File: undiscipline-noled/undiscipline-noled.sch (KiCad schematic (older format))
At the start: 177 parts, among them J2 USB_B_Micro, SW1 SW_Push, SW10 SW_Push, SW11 SW_Push, SW12 SW_Push, SW13 SW_Push, SW14 SW_Push, SW15 SW_Push, SW16 SW_Push, SW17 SW_Push, SW18 SW_Push, SW19 SW_Push, SW2 SW_Push, SW20 SW_Push, SW21 SW_Push, SW22 SW_Push, SW23 SW_Push, SW24 SW_Push, SW25 SW_Push, SW26 SW_Push, SW27 SW_Push, SW28 SW_Push, SW29 SW_Push, SW3 SW_Push, SW30 SW_Push, SW31 SW_Push, SW32 SW_Push, SW33 SW_Push, SW34 SW_Push, SW35 SW_Push, SW36 SW_Push, SW37 SW_Push, SW38 SW_Push, SW39 SW_Push, SW4 SW_Push, SW40 SW_Push, SW41 SW_Push, SW42 SW_Push, SW43 SW_Push, SW44 SW_Push, SW45 SW_Push, SW46 SW_Push, SW47 SW_Push, SW48 SW_Push, SW49 SW_Push, SW5 SW_Push, SW50 SW_Push, SW51 SW_Push, SW52 SW_Push, SW53 SW_Push, SW54 SW_Push, SW55 SW_Push, SW56 SW_Push, SW57 SW_Push, SW58 SW_Push, SW59 SW_Push, SW6 SW_Push, SW60 SW_Push, SW61 SW_Push, SW62 SW_Push, SW63 SW_Push, SW64 SW_Push, SW65 SW_Push, SW66 SW_Push, SW67 SW_Push, SW68 SW_Push, SW69 SW_Push, SW7 SW_Push, SW70 SW_Push, SW71 SW_Push, SW72 SW_Push, SW73 SW_Push, SW74 SW_Push, SW75 SW_Push, SW8 SW_Push, SW9 SW_Push, U1 ATmega32A-PU, Y1 16MHz

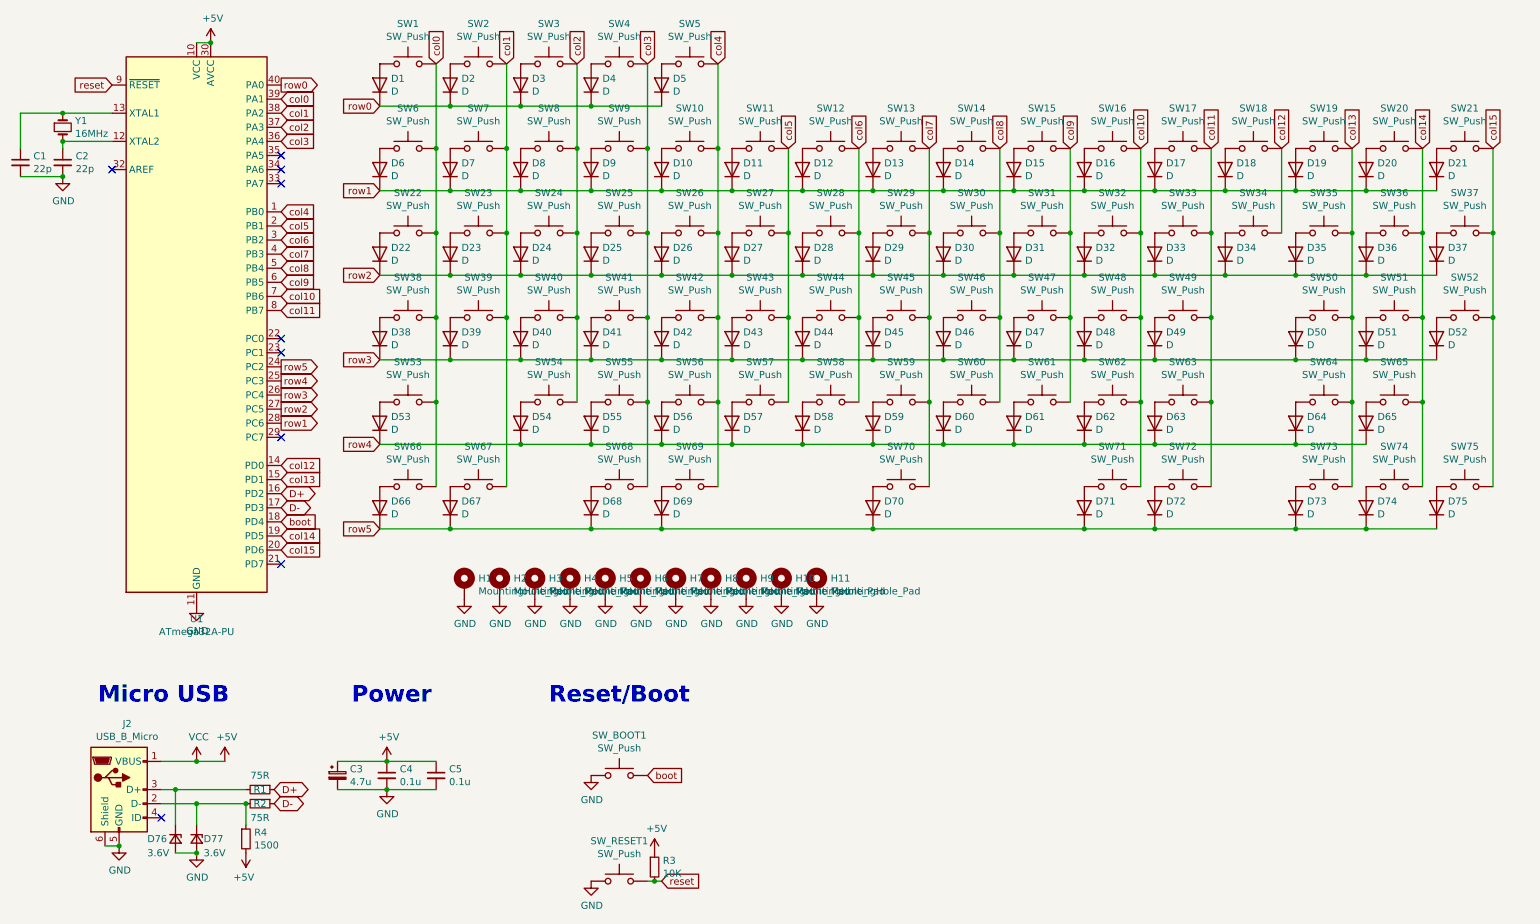
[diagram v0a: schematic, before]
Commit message: Add plates
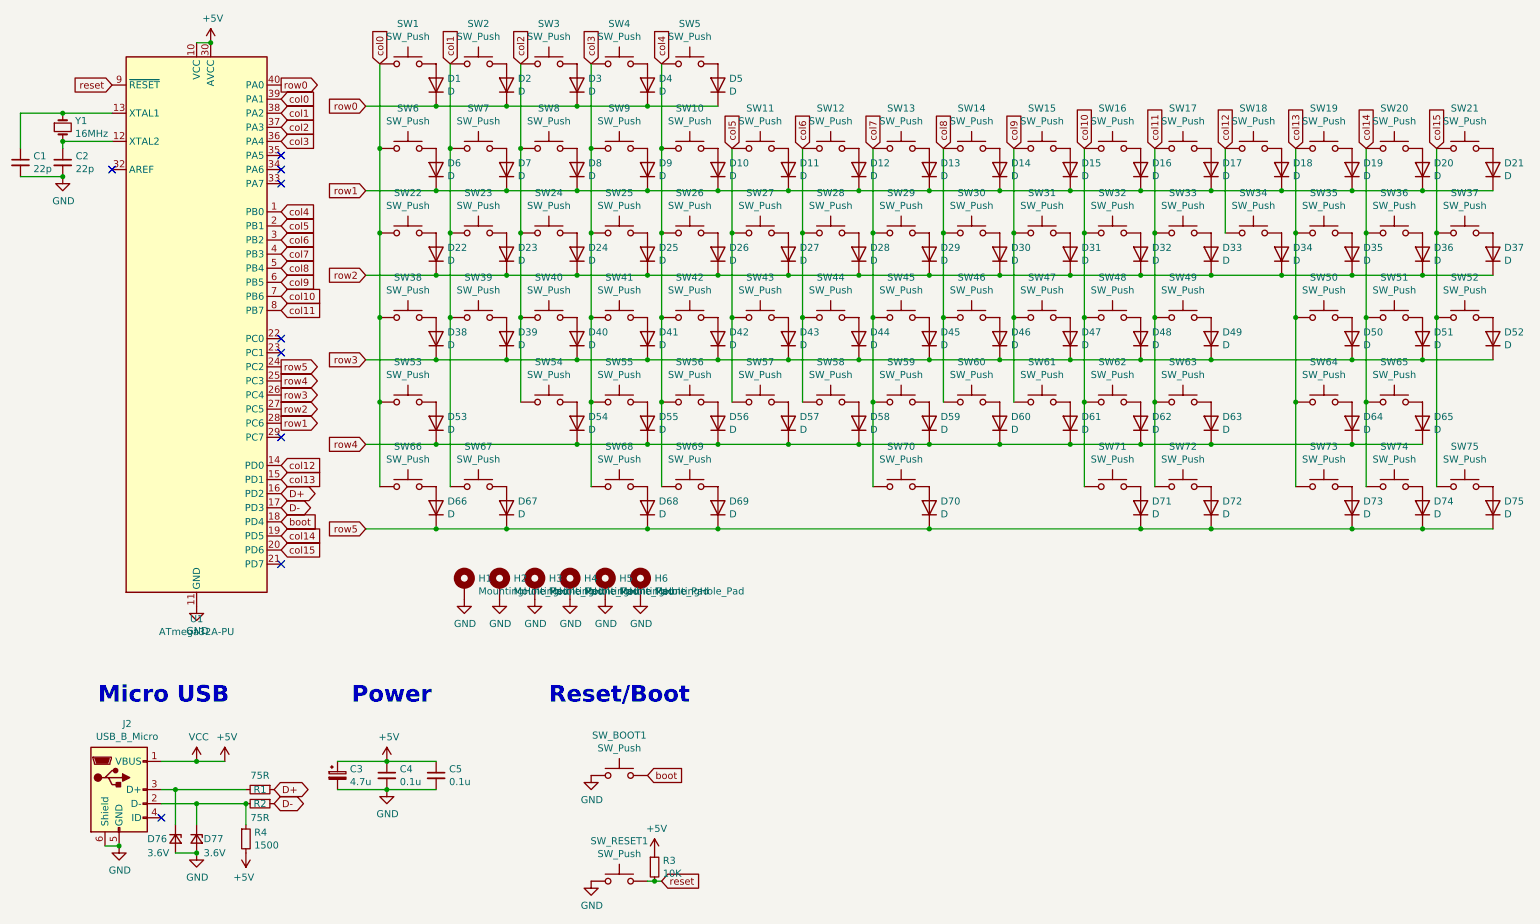
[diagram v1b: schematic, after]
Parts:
- removed H10, H11, H7, H8, H9: MountingHole_Pad, MountingHole:MountingHole_2.2mm_M2_DIN965_Pad_TopBottom, symbol Mechanical:MountingHole_Pad
- SW1, SW10, SW11, SW12, SW13, SW14, SW15, SW16, SW17, SW18, SW2, SW20, SW21, SW23, SW24, SW25, SW26, SW27, SW28, SW29, SW3, SW30, SW31, SW32, SW33, SW34, SW36, SW37, SW39, SW4, SW40, SW41, SW42, SW43, SW44, SW45, SW46, SW47, SW48, SW49, SW5, SW51, SW52, SW53, SW54, SW55, SW56, SW57, SW58, SW59, SW6, SW60, SW61, SW62, SW63, SW65, SW7, SW73, SW74, SW75, SW8, SW9: footprint keyboard-parts:CherryMX_Kailh_Socket -> Button_Switch_Keyboard:SW_Cherry_MX_1.00u_Plate
- SW19: footprint keyboard-parts:CherryMX_Kailh_Socket -> Button_Switch_Keyboard:SW_Cherry_MX_2.00u_Plate
- SW22, SW35: footprint keyboard-parts:CherryMX_Kailh_Socket -> Button_Switch_Keyboard:SW_Cherry_MX_1.50u_Plate
- SW38: footprint keyboard-parts:CherryMX_Kailh_Socket -> Button_Switch_Keyboard:SW_Cherry_MX_1.75u_Plate
- SW50: footprint keyboard-parts:CherryMX_Kailh_Socket -> Button_Switch_Keyboard:SW_Cherry_MX_2.25u_Plate
- SW64: footprint keyboard-parts:CherryMX_Kailh_Socket -> Button_Switch_Keyboard:SW_Cherry_MX_2.75u_Plate
- SW66, SW67, SW68, SW69, SW71, SW72: footprint keyboard-parts:CherryMX_Kailh_Socket -> Button_Switch_Keyboard:SW_Cherry_MX_1.25u_Plate
- SW70: footprint keyboard-parts:CherryMX_Kailh_Socket -> Button_Switch_Keyboard:SW_Cherry_MX_6.25u_Plate
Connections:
- net col0: now also SW1.1, SW22.1, SW38.1, SW53.1, SW6.1, SW66.1; no longer SW1.2, SW22.2, SW38.2, SW53.2, SW6.2, SW66.2
- net col1: now also SW2.1, SW23.1, SW39.1, SW67.1, SW7.1; no longer SW2.2, SW23.2, SW39.2, SW67.2, SW7.2
- net col10: now also SW16.1, SW32.1, SW48.1, SW62.1, SW71.1; no longer SW16.2, SW32.2, SW48.2, SW62.2, SW71.2
- net col11: now also SW17.1, SW33.1, SW49.1, SW63.1, SW72.1; no longer SW17.2, SW33.2, SW49.2, SW63.2, SW72.2
- net col12: now also SW18.1, SW34.1; no longer SW18.2, SW34.2
- net col13: now also SW19.1, SW35.1, SW50.1, SW64.1, SW73.1; no longer SW19.2, SW35.2, SW50.2, SW64.2, SW73.2
- net col14: now also SW20.1, SW36.1, SW51.1, SW65.1, SW74.1; no longer SW20.2, SW36.2, SW51.2, SW65.2, SW74.2
- net col15: now also SW21.1, SW37.1, SW52.1, SW75.1; no longer SW21.2, SW37.2, SW52.2, SW75.2
- net col2: now also SW24.1, SW3.1, SW40.1, SW54.1, SW8.1; no longer SW24.2, SW3.2, SW40.2, SW54.2, SW8.2
- net col3: now also SW25.1, SW4.1, SW41.1, SW55.1, SW68.1, SW9.1; no longer SW25.2, SW4.2, SW41.2, SW55.2, SW68.2, SW9.2
- net col4: now also SW10.1, SW26.1, SW42.1, SW5.1, SW56.1, SW69.1; no longer SW10.2, SW26.2, SW42.2, SW5.2, SW56.2, SW69.2
- net col5: now also SW11.1, SW27.1, SW43.1, SW57.1; no longer SW11.2, SW27.2, SW43.2, SW57.2
- net col6: now also SW12.1, SW28.1, SW44.1, SW58.1; no longer SW12.2, SW28.2, SW44.2, SW58.2
- net col7: now also SW13.1, SW29.1, SW45.1, SW59.1, SW70.1; no longer SW13.2, SW29.2, SW45.2, SW59.2, SW70.2
- net col8: now also SW14.1, SW30.1, SW46.1, SW60.1; no longer SW14.2, SW30.2, SW46.2, SW60.2
- net col9: now also SW15.1, SW31.1, SW47.1, SW61.1; no longer SW15.2, SW31.2, SW47.2, SW61.2
- net at D6.2 (A): now also SW6.2; no longer SW6.1
- net at D7.2 (A): now also SW7.2; no longer SW7.1
- net at D8.2 (A): now also SW8.2; no longer SW8.1
- net at D9.2 (A): now also SW9.2; no longer SW9.1
- net at D10.2 (A): now also SW10.2; no longer SW10.1
- net at D11.2 (A): now also SW11.2; no longer SW11.1
- net at D12.2 (A): now also SW12.2; no longer SW12.1
- net at D13.2 (A): now also SW13.2; no longer SW13.1
- net at D14.2 (A): now also SW14.2; no longer SW14.1
- net at D15.2 (A): now also SW15.2; no longer SW15.1
- net at D16.2 (A): now also SW16.2; no longer SW16.1
- net at D17.2 (A): now also SW17.2; no longer SW17.1
- net at D18.2 (A): now also SW18.2; no longer SW18.1
- net at D19.2 (A): now also SW19.2; no longer SW19.1
- net at D20.2 (A): now also SW20.2; no longer SW20.1
- net at D22.2 (A): now also SW22.2; no longer SW22.1
- net at D23.2 (A): now also SW23.2; no longer SW23.1
- net at D24.2 (A): now also SW24.2; no longer SW24.1
- net at D25.2 (A): now also SW25.2; no longer SW25.1
- net at D26.2 (A): now also SW26.2; no longer SW26.1
- net at D27.2 (A): now also SW27.2; no longer SW27.1
- net at D28.2 (A): now also SW28.2; no longer SW28.1
- net at D29.2 (A): now also SW29.2; no longer SW29.1
- net at D30.2 (A): now also SW30.2; no longer SW30.1
- net at D31.2 (A): now also SW31.2; no longer SW31.1
- net at D32.2 (A): now also SW32.2; no longer SW32.1
- net at D33.2 (A): now also SW33.2; no longer SW33.1
- net at D34.2 (A): now also SW34.2; no longer SW34.1
- net at D35.2 (A): now also SW35.2; no longer SW35.1
- net at D36.2 (A): now also SW36.2; no longer SW36.1
- net at D38.2 (A): now also SW38.2; no longer SW38.1
- net at D39.2 (A): now also SW39.2; no longer SW39.1
- net at D40.2 (A): now also SW40.2; no longer SW40.1
- net at D41.2 (A): now also SW41.2; no longer SW41.1
- net at D42.2 (A): now also SW42.2; no longer SW42.1
- net at D43.2 (A): now also SW43.2; no longer SW43.1
- net at D44.2 (A): now also SW44.2; no longer SW44.1
- net at D45.2 (A): now also SW45.2; no longer SW45.1
- net at D46.2 (A): now also SW46.2; no longer SW46.1
- net at D47.2 (A): now also SW47.2; no longer SW47.1
- net at D48.2 (A): now also SW48.2; no longer SW48.1
- net at D49.2 (A): now also SW49.2; no longer SW49.1
- net at D50.2 (A): now also SW50.2; no longer SW50.1
- net at D51.2 (A): now also SW51.2; no longer SW51.1
- net at D53.2 (A): now also SW53.2; no longer SW53.1
- net at D54.2 (A): now also SW54.2; no longer SW54.1
- net at D55.2 (A): now also SW55.2; no longer SW55.1
- net at D56.2 (A): now also SW56.2; no longer SW56.1
- net at D57.2 (A): now also SW57.2; no longer SW57.1
- net at D58.2 (A): now also SW58.2; no longer SW58.1
- net at D59.2 (A): now also SW59.2; no longer SW59.1
- net at D60.2 (A): now also SW60.2; no longer SW60.1
- net at D61.2 (A): now also SW61.2; no longer SW61.1
- net at D62.2 (A): now also SW62.2; no longer SW62.1
- net at D63.2 (A): now also SW63.2; no longer SW63.1
- net at D64.2 (A): now also SW64.2; no longer SW64.1
- net at D65.2 (A): now also SW65.2; no longer SW65.1
- net at D66.2 (A): now also SW66.2; no longer SW66.1
- net at D67.2 (A): now also SW67.2; no longer SW67.1
- net at D68.2 (A): now also SW68.2; no longer SW68.1
- net at D70.2 (A): now also SW70.2; no longer SW70.1
- net at D71.2 (A): now also SW71.2; no longer SW71.1
- net at D72.2 (A): now also SW72.2; no longer SW72.1
- net at D73.2 (A): now also SW73.2; no longer SW73.1
- net at D74.2 (A): now also SW74.2; no longer SW74.1
- net at D21.2 (A): now also SW21.2; no longer SW21.1
- net at D37.2 (A): now also SW37.2; no longer SW37.1
- net at D52.2 (A): now also SW52.2; no longer SW52.1
- net at D75.2 (A): now also SW75.2; no longer SW75.1
- net at D1.2 (A): now also SW1.2; no longer SW1.1
- net at D2.2 (A): now also SW2.2; no longer SW2.1
- net at D69.2 (A): now also SW69.2; no longer SW69.1
- net at D3.2 (A): now also SW3.2; no longer SW3.1
- net at D4.2 (A): now also SW4.2; no longer SW4.1
- net at D5.2 (A): now also SW5.2; no longer SW5.1
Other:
- moved on the sheet: D1, D10, D11, D12, D13, D14, D15, D16, D17, D18, D19, D2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
